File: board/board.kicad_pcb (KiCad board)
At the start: 2 copper layers, 36.5 x 17.5 mm, 39 parts, among them J2 Conn_01x10, J3 Conn_01x06, J4 Conn_01x02, J7 Conn_01x30, J8 USB_C_Receptacle_USB2.0_16P, J9 Conn_01x02, U2 nPM1300-QEAA, U3 MDBT50Q-P1MV2, U4 TVS_Array, Y1 32k Hz

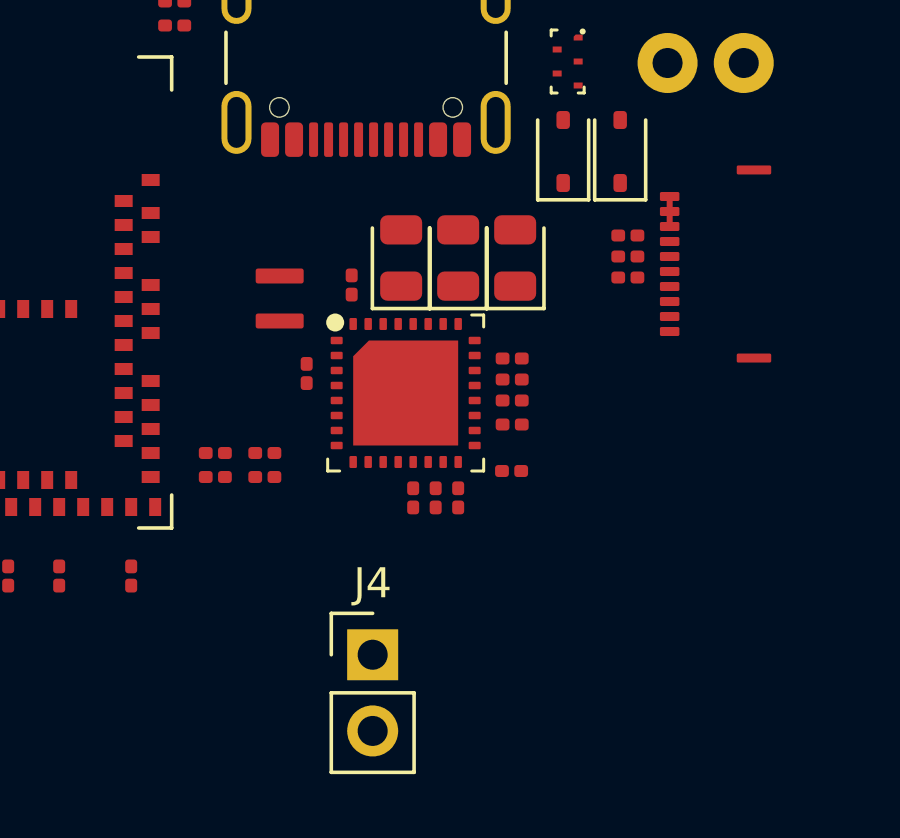
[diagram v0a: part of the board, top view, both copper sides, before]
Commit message: board: pcb route pmic power
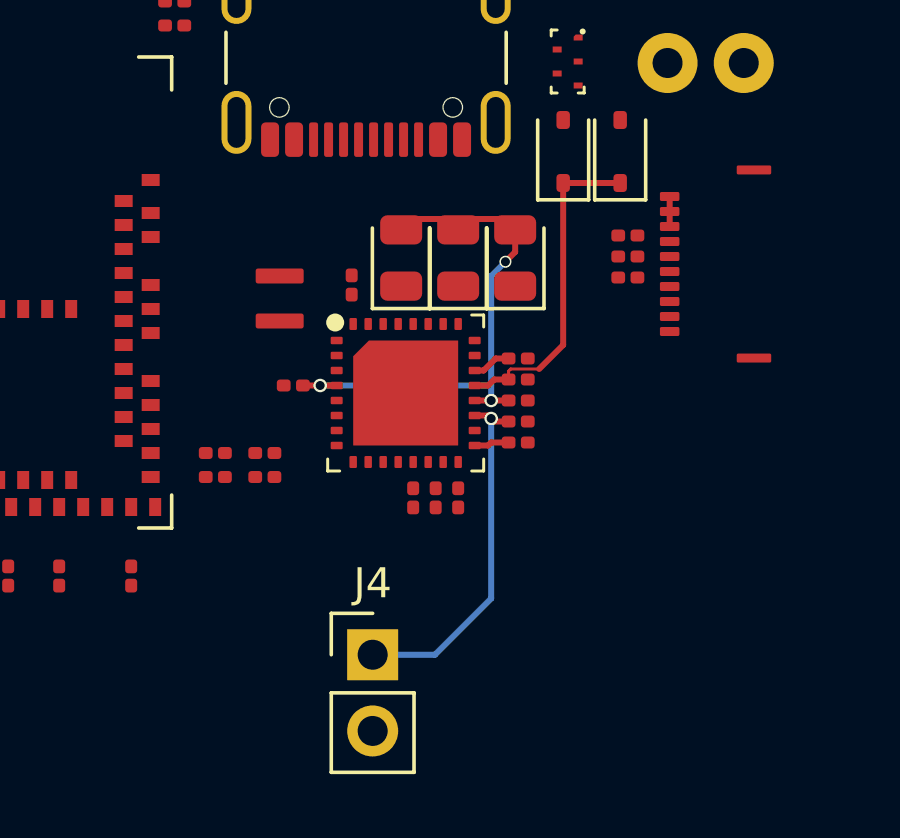
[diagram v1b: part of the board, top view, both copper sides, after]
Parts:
- moved R10 0.98 mm to (116.8, 63.0)
- moved C16 0.60 mm to (109.3, 61.0), turned to 180 degrees
- moved C13 0.22 mm to (116.8, 62.2)
- moved C12 0.20 mm to (116.8, 60.9)
- moved C14 0.20 mm to (116.8, 60.1)
- moved C15 0.20 mm to (116.8, 61.5)
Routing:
- net vsys: track 0.00 -> 18.1 mm, vias 0 -> 3
- net vbat: track 0.00 -> 11.9 mm, vias 0 -> 1
- net vbus_raw: track 0.00 -> 11.0 mm
- net vbus: track 0.00 -> 1.30 mm
- net Net-(U2-VSET1): track 0.00 -> 1.17 mm

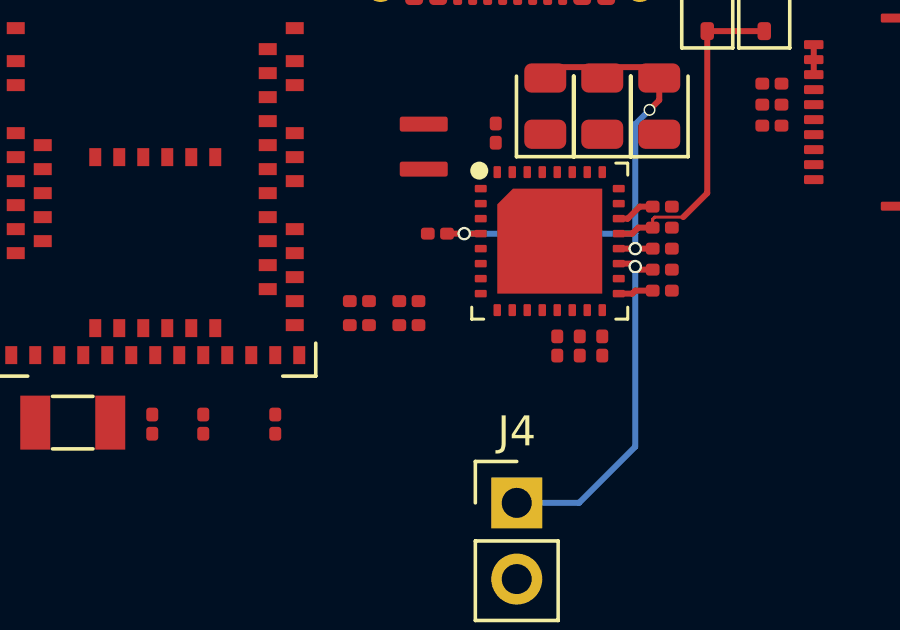
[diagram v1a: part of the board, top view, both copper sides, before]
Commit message: board: pcb route pmic i2c
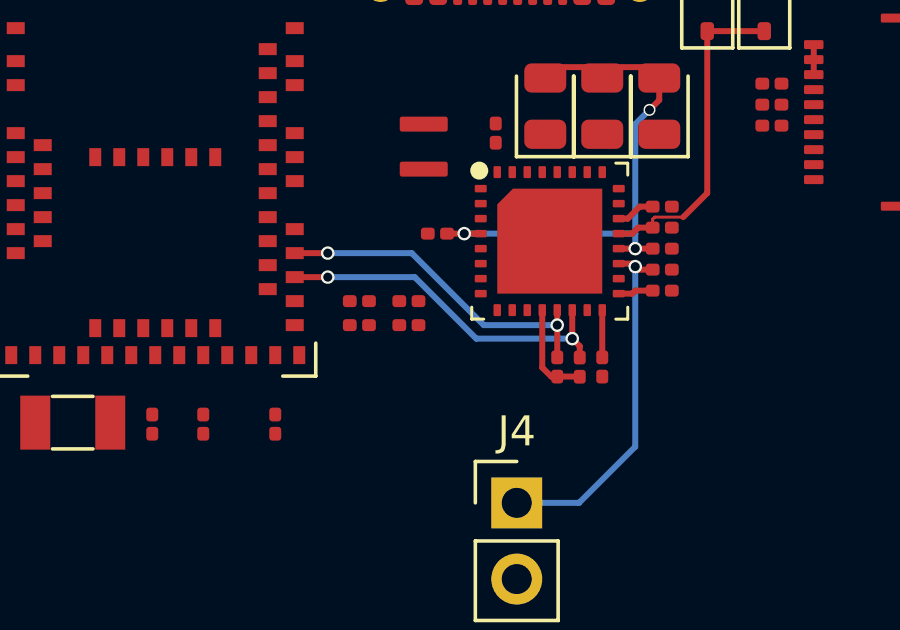
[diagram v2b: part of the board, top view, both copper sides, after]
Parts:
- moved R13 0.70 mm to (114.0, 65.5)
- moved R11 0.70 mm to (114.8, 65.5)
- moved R12 0.70 mm to (113.2, 65.5)
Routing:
- net scl: track 0.00 -> 11.8 mm, vias 0 -> 2
- net sda: track 0.00 -> 11.3 mm, vias 0 -> 2
- net +3V3: track 0.00 -> 3.29 mm
- net Net-(U2-VSET2): track 0.00 -> 1.57 mm
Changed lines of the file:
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@@
 	(footprint "Resistor_SMD:R_0201_0603Metric"
 		(layer "F.Cu")
-		(at 114.75 64.795 90)
+		(at 114.75 65.495 90)
 		(descr "Resistor SMD 0201 (0603 Metric), square (rectangular) end terminal, IPC-7351 nominal, (Body size source: https://www.vishay.com/docs/20052/crcw0201e3.pdf), generated with kicad-footprint-generator")
 		(tags "resistor")
@@
 	(footprint "Resistor_SMD:R_0201_0603Metric"
 		(layer "F.Cu")
-		(at 114 64.795 90)
+		(at 114 65.5 90)
 		(descr "Resistor SMD 0201 (0603 Metric), square (rectangular) end terminal, IPC-7351 nominal, (Body size source: https://www.vishay.com/docs/20052/crcw0201e3.pdf), generated with kicad-footprint-generator")
 		(tags "resistor")
@@
 		)
 		(fp_text user "${REFERENCE}"
-			(at 0 3.4 0)
+			(at -1.05 3.4 0)
 			(unlocked yes)
 			(layer "F.Fab")
@@
 	(footprint "Resistor_SMD:R_0201_0603Metric"
 		(layer "F.Cu")
-		(at 113.25 64.795 90)
+		(at 113.25 65.495 90)
 		(descr "Resistor SMD 0201 (0603 Metric), square (rectangular) end terminal, IPC-7351 nominal, (Body size source: https://www.vishay.com/docs/20052/crcw0201e3.pdf), generated with kicad-footprint-generator")
 		(tags "resistor")
@@
 	)
 	(segment
+		(start 114.75 63.6)
+		(end 114.75 65.175)
+		(width 0.2)
+		(layer "F.Cu")
+		(net 17)
+	)
+	(segment
+		(start 113.25 63.6)
+		(end 113.25 64.1)
+		(width 0.2)
+		(layer "F.Cu")
+		(net 18)
+	)
+	(segment
+		(start 113.25 64.1)
+		(end 113.25 65.175)
+		(width 0.2)
+		(layer "F.Cu")
+		(net 18)
+	)
+	(segment
+		(start 104.5 61.7)
+		(end 105.6 61.7)
+		(width 0.2)
+		(layer "F.Cu")
+		(net 18)
+	)
+	(via
+		(at 105.6 61.7)
+		(size 0.45)
+		(drill 0.3)
+		(layers "F.Cu" "B.Cu")
+		(net 18)
+	)
+	(via
+		(at 113.25 64.1)
+		(size 0.45)
+		(drill 0.3)
+		(layers "F.Cu" "B.Cu")
+		(net 18)
+	)
+	(segment
+		(start 113.25 64.1)
+		(end 110.8 64.1)
+		(width 0.2)
+		(layer "B.Cu")
+		(net 18)
+	)
+	(segment
+		(start 108.4 61.7)
+		(end 105.6 61.7)
+		(width 0.2)
+		(layer "B.Cu")
+		(net 18)
+	)
+	(segment
+		(start 110.8 64.1)
+		(end 108.4 61.7)
+		(width 0.2)
+		(layer "B.Cu")
+		(net 18)
+	)
+	(segment
+		(start 114 64.8)
+		(end 113.75 64.55)
+		(width 0.2)
+		(layer "F.Cu")
+		(net 19)
+	)
+	(segment
+		(start 113.75 63.6)
+		(end 113.75 64.55)
+		(width 0.2)
+		(layer "F.Cu")
+		(net 19)
+	)
+	(segment
+		(start 104.5 62.5)
+		(end 105.6 62.5)
+		(width 0.2)
+		(layer "F.Cu")
+		(net 19)
+	)
+	(segment
+		(start 114 65.175)
+		(end 114 64.8)
+		(width 0.2)
+		(layer "F.Cu")
+		(net 19)
+	)
+	(via
+		(at 105.6 62.5)
+		(size 0.45)
+		(drill 0.3)
+		(layers "F.Cu" "B.Cu")
+		(net 19)
+	)
+	(via
+		(at 113.75 64.55)
+		(size 0.45)
+		(drill 0.3)
+		(layers "F.Cu" "B.Cu")
+		(net 19)
+	)
+	(segment
+		(start 108.5 62.5)
+		(end 105.6 62.5)
+		(width 0.2)
+		(layer "B.Cu")
+		(net 19)
+	)
+	(segment
+		(start 113.75 64.55)
+		(end 110.55 64.55)
+		(width 0.2)
+		(layer "B.Cu")
+		(net 19)
+	)
+	(segment
+		(start 110.55 64.55)
+		(end 108.5 62.5)
+		(width 0.2)
+		(layer "B.Cu")
+		(net 19)
+	)
+	(segment
 		(start 121.8 54.75)
 		(end 121.8 55.75)
@@
 	)
 	(segment
+		(start 113.050001 65.815)
+		(end 114 65.815)
+		(width 0.2)
+		(layer "F.Cu")
+		(net 46)
+	)
+	(segment
+		(start 112.75 65.514999)
+		(end 113.050001 65.815)
+		(width 0.2)
+		(layer "F.Cu")
+		(net 46)
+	)
+	(segment
+		(start 112.75 63.6)
+		(end 112.75 65.514999)
+		(width 0.2)
+		(layer "F.Cu")
+		(net 46)
+	)
+	(segment

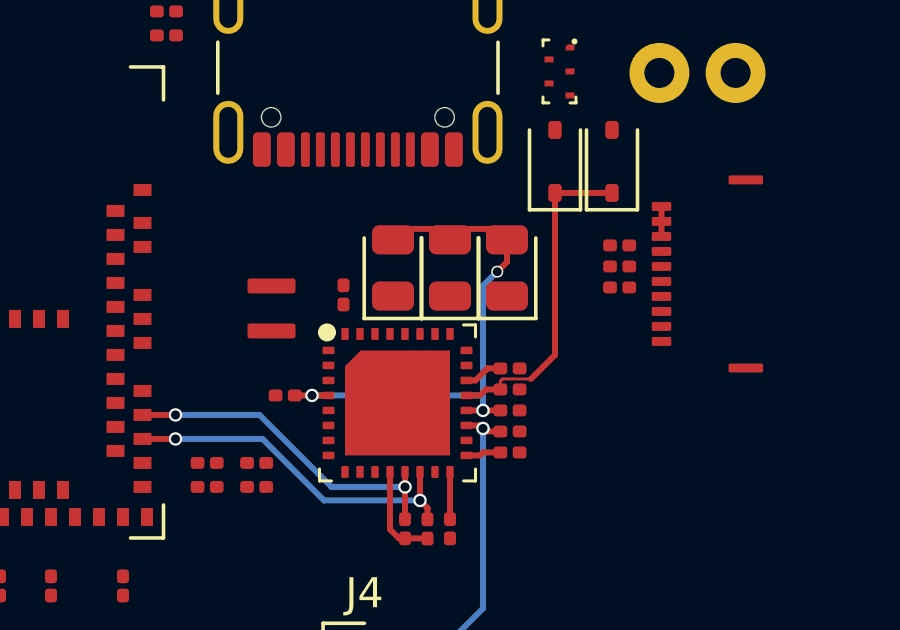
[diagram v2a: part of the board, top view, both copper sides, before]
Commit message: board: pcb route pmic led
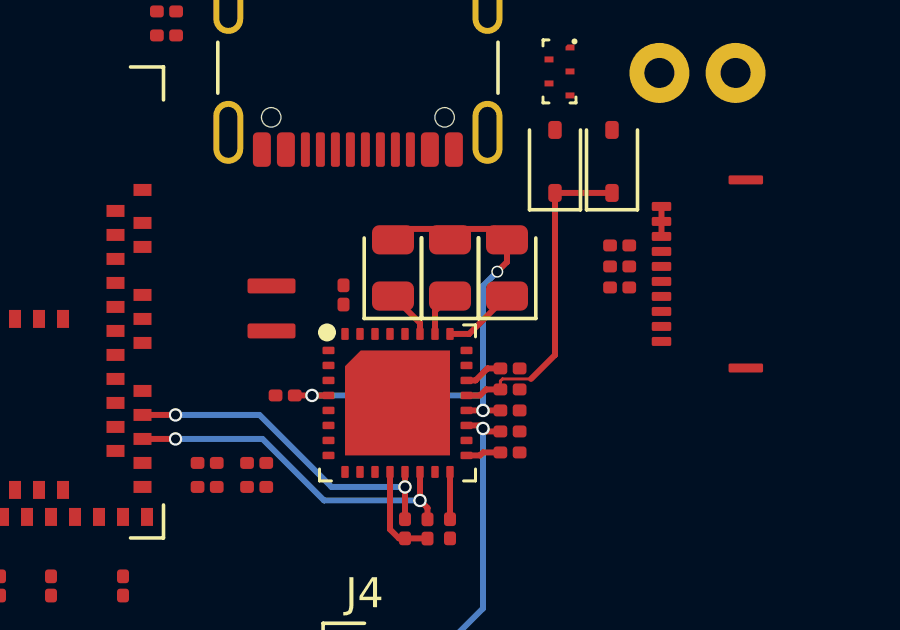
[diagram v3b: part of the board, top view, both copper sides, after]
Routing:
- net Net-(D6-K): track 0.00 -> 2.42 mm
- net Net-(D8-K): track 0.00 -> 1.64 mm
- net Net-(D7-K): track 0.00 -> 1.47 mm
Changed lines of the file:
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@@
+	)
+	(segment
+		(start 115.3875 59)
+		(end 114.75 59)
+		(width 0.2)
+		(layer "F.Cu")
+		(net 7)
+	)
+	(segment
+		(start 116.65 57.7375)
+		(end 115.3875 59)
+		(width 0.2)
+		(layer "F.Cu")
+		(net 7)
+	)
+	(segment
+		(start 114.75 57.7375)
+		(end 114.25 58.2375)
+		(width 0.2)
+		(layer "F.Cu")
+		(net 8)
+	)
+	(segment
+		(start 114.25 58.2375)
+		(end 114.25 59)
+		(width 0.2)
+		(layer "F.Cu")
+		(net 8)
+	)
+	(segment
+		(start 112.85 57.7375)
+		(end 113.75 58.6375)
+		(width 0.2)
+		(layer "F.Cu")
+		(net 9)
+	)
+	(segment
+		(start 113.75 58.6375)
+		(end 113.75 59)
+		(width 0.2)
+		(layer "F.Cu")
+		(net 9)
 	)
 	(segment

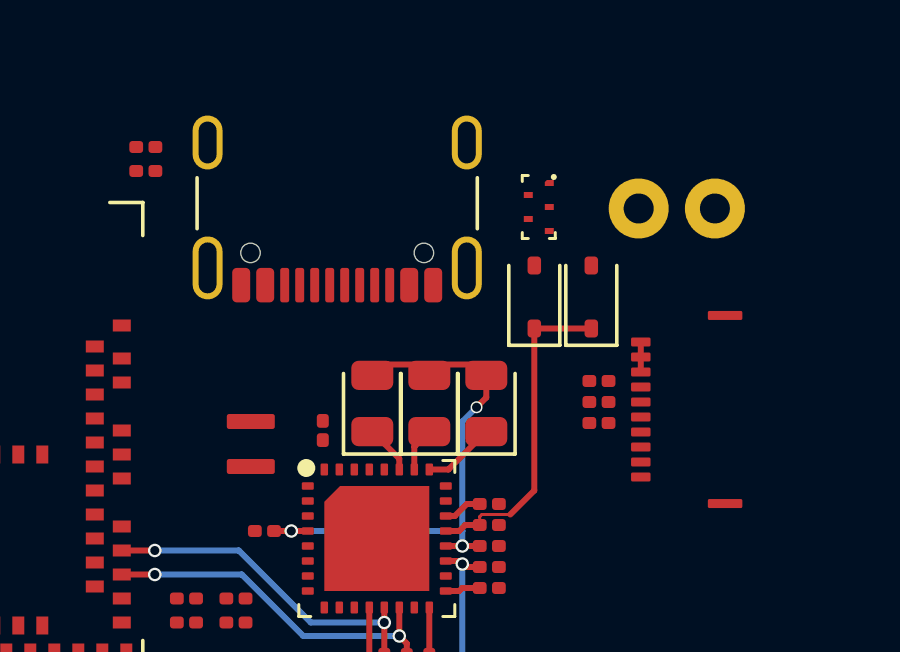
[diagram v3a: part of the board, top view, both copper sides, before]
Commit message: board: pcb route vbus_raw
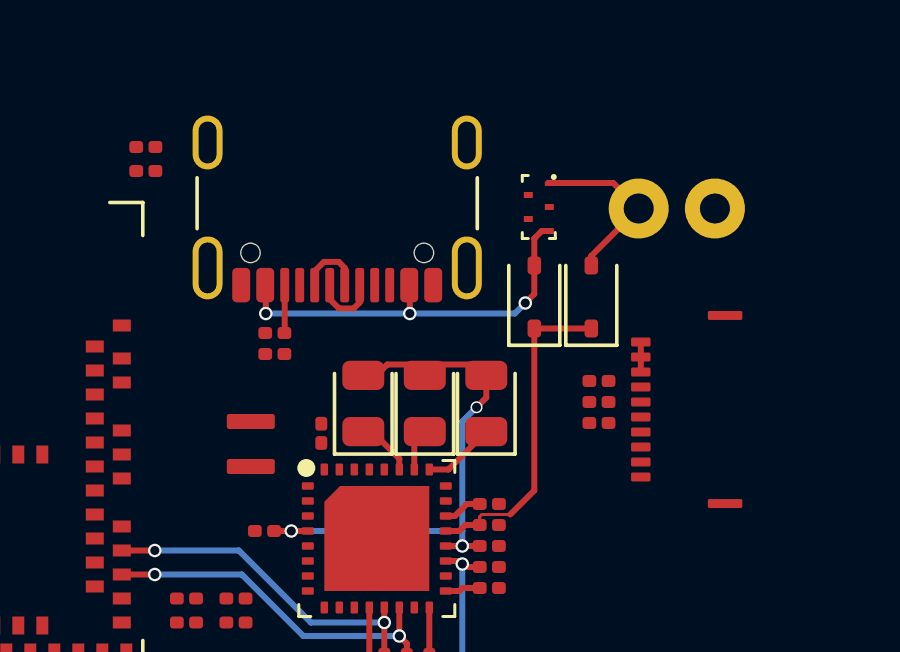
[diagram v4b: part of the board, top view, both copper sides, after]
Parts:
- added R14: 5.1kR, Resistor_SMD:R_0201_0603Metric, F.Cu at (109.6, 54.5)
- added R4: 5.1kR, Resistor_SMD:R_0201_0603Metric, F.Cu at (109.6, 55.1)
- moved D8 0.30 mm to (112.5, 56.8)
- moved D7 0.15 mm to (114.6, 56.8)
- moved C17 0.11 mm to (111.2, 57.8)
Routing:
- net Net-(D3-A): track 0.00 -> 13.6 mm, vias 0 -> 3
- net Net-(D4-A): track 0.00 -> 5.89 mm
- net usbd-: track 0.00 -> 2.25 mm
- net usbd+: track 0.00 -> 2.25 mm
- net Net-(J8-CC2): track 0.00 -> 1.60 mm
- net Net-(D7-K): track 1.47 -> 0.91 mm
